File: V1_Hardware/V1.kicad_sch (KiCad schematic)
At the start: 20 parts, among them J1 Conn_01x04_Pin, P1 USB_C_Plug_USB2.0, SW1 SW_SPDT, U1 STM32F446RETx, Y1 8MHz

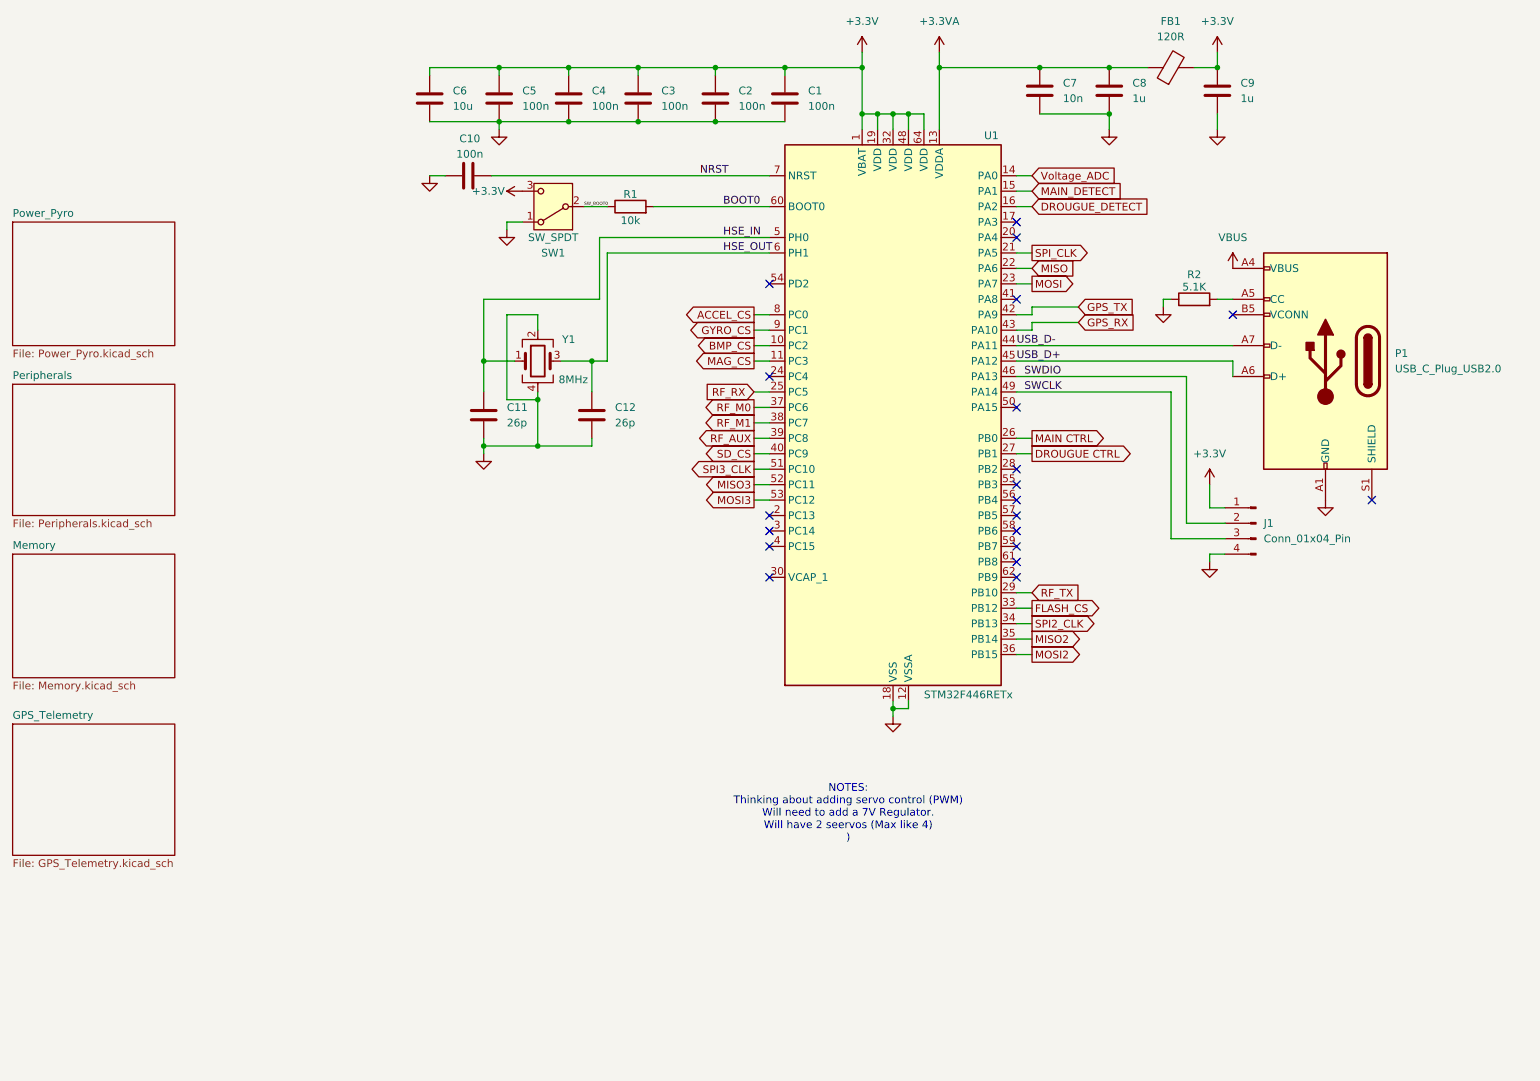
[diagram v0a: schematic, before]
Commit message: added the V1 to personal repo from org repo
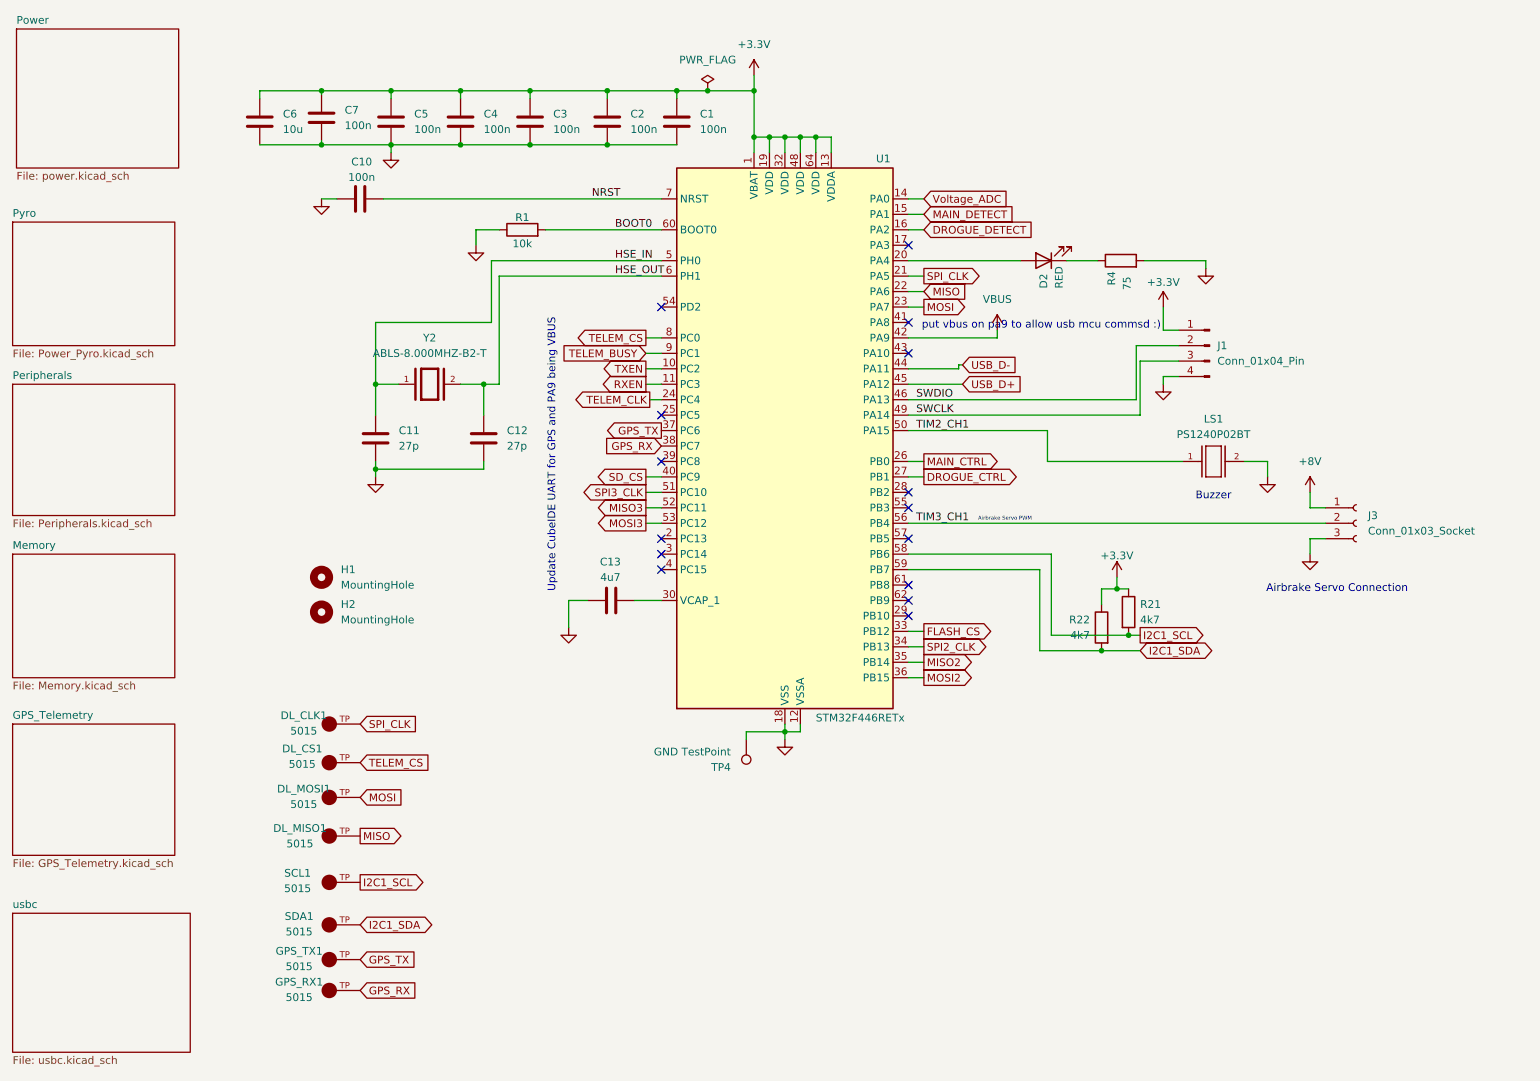
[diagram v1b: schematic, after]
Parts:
- removed C8, C9: 1u, symbol Device:C
- removed FB1: 120R, symbol Device:FerriteBead
- removed P1: USB_C_Plug_USB2.0, symbol Connector:USB_C_Plug_USB2.0
- removed R2: 5.1K, symbol Device:R
- removed SW1: SW_SPDT, symbol Switch:SW_SPDT
- removed Y1: 8MHz, symbol Device:Crystal_GND24
- added C13: 4u7, Capacitor_SMD:C_0603_1608Metric_Pad1.08x0.95mm_HandSolder, symbol Device:C
- added D2: RED, LED_SMD:LED_1206_3216Metric_Pad1.42x1.75mm_HandSolder, symbol Device:LED
- added DL_CLK1, DL_CS1, DL_MISO1, DL_MOSI1, GPS_RX1, GPS_TX1, SCL1, SDA1: 5015, V1:5015, symbol 5015:5015
- added H1, H2: MountingHole, MountingHole:MountingHole_3.2mm_M3, symbol Mechanical:MountingHole
- added J3: Conn_01x03_Socket, Connector_Molex:Molex_Nano-Fit_105309-xx03_1x03_P2.50mm_Vertical, symbol Connector:Conn_01x03_Socket
- added LS1: PS1240P02BT, V1:PS1240P02BT, symbol PS1240P02BT:PS1240P02BT
- added R21, R22: 4k7, Resistor_SMD:R_0603_1608Metric_Pad0.98x0.95mm_HandSolder, symbol Device:R
- added R4: 75, Resistor_SMD:R_0603_1608Metric_Pad0.98x0.95mm_HandSolder, symbol Device:R
- added TP4: GND TestPoint, TestPoint:TestPoint_Pad_D2.0mm, symbol Connector:TestPoint
- added Y2: ABLS-8.000MHZ-B2-T, V1:ABLS-8.000MHZ-B2-T, symbol ABLS-8.000MHZ-B2-T:ABLS-8.000MHZ-B2-T
- C1, C10, C2, C3, C4, C5, C6: footprint (none) -> Capacitor_SMD:C_0603_1608Metric_Pad1.08x0.95mm_HandSolder
- C11, C12: value 26p -> 27p; footprint (none) -> Capacitor_SMD:C_0603_1608Metric_Pad1.08x0.95mm_HandSolder
- C7: value 10n -> 100n; footprint (none) -> Capacitor_SMD:C_0603_1608Metric_Pad1.08x0.95mm_HandSolder
- J1: footprint (none) -> Connector_PinHeader_2.54mm:PinHeader_1x04_P2.54mm_Vertical
- R1: footprint (none) -> Resistor_SMD:R_0603_1608Metric_Pad0.98x0.95mm_HandSolder
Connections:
- net +3.3VA is gone; now on net +3.3V: C7.1, U1.13 (VDDA)
- net RF_M0 is gone; now on net GPS_TX: U1.37 (PC6)
- net RF_M1 is gone; now on net GPS_RX: U1.38 (PC7)
- net SW_BOOT0 is gone; now on net GND: R1.1
- net +3.3V: now also R21.1, R22.1
- net GND: now also C13.1, J3.3 (Pin_3), LS1.2, R4.2, TP4.1
- net GPS_RX: now also GPS_RX1.TP; no longer U1.43 (PA10)
- net GPS_TX: now also GPS_TX1.TP; no longer U1.42 (PA9)
- net HSE_IN: now also Y2.1
- net HSE_OUT: now also Y2.2
- net MISO: now also DL_MISO1.TP
- net MOSI: now also DL_MOSI1.TP
- net SPI_CLK: now also DL_CLK1.TP
- net VBUS: now also U1.42 (PA9)
- net at U1.20 (PA4): now also D2.2 (A)
- net TELEM_CLK: now reaches U1.24 (PC4)
- net at U1.30 (VCAP_1): now also C13.2
- net TIM2_CH1: now reaches U1.50 (PA15)
- net TIM2_CH1: now also LS1.1
- net TIM3_CH1: now reaches U1.56 (PB4)
- net TIM3_CH1: now also J3.2 (Pin_2)
- net I2C1_SCL: now reaches U1.58 (PB6)
- net I2C1_SCL: now also R21.2, SCL1.TP
- net I2C1_SDA: now reaches U1.59 (PB7)
- net I2C1_SDA: now also R22.2, SDA1.TP
- net ACCEL_CS renamed TELEM_CS
- net TELEM_CS: now also DL_CS1.TP
- net BMP_CS renamed TXEN
- net DROUGUE CTRL renamed DROGUE_CTRL
- net DROUGUE_DETECT renamed DROGUE_DETECT
- net GYRO_CS renamed TELEM_BUSY
- net MAG_CS renamed RXEN
- net MAIN CTRL renamed MAIN_CTRL
- net RF_AUX: no longer names the net of U1.39 (PC8)
- net RF_RX: no longer names the net of U1.25 (PC5)
- net RF_TX: no longer names the net of U1.29 (PB10)
- new net: D2.1 (K), R4.1
- new net +8V: J3.1 (Pin_1)
- no-connect marks 20 -> 15
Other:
- sheet Power_Pyro renamed Pyro
- added sheet Power (power.kicad_sch)
- added sheet usbc (usbc.kicad_sch)
- note added: "Airbrake Servo Connection"
- note added: "Airbrake Servo PWM"
- note added: "Buzzer"
- note added: "Update CubeIDE UART for GPS and PA9 being VBUS"
- note added: "put vbus on pa9 to allow usb mcu commsd :)"
- note removed: "NOTES: Thinking about adding servo control (PWM) Will need to add a 7V Regulator. Will have 2 seervos (Max like 4) )"
- moved on the sheet: C1, C10, C11, C12, C2, C3, C4, C5, C6, J1, R1, U1
